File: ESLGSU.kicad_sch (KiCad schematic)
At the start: 3 parts, among them J1 Barrel_Jack_Switch, U1 TCA9544A

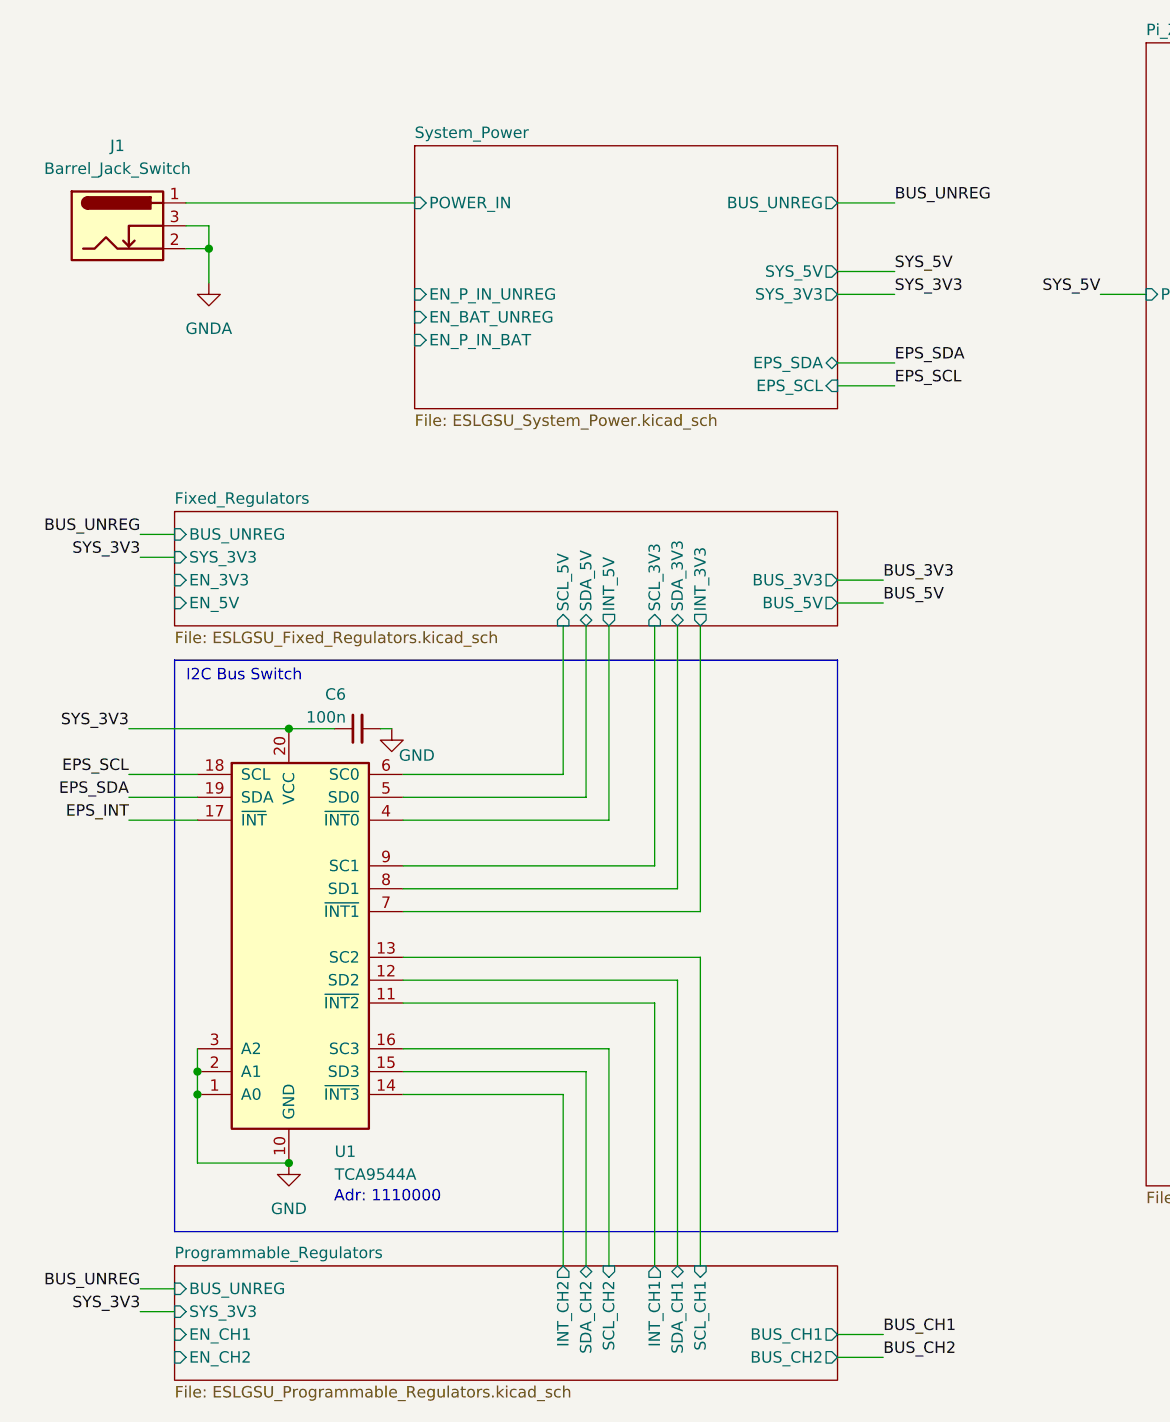
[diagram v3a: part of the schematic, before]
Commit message: Added 5v/3V3 regulators and mux
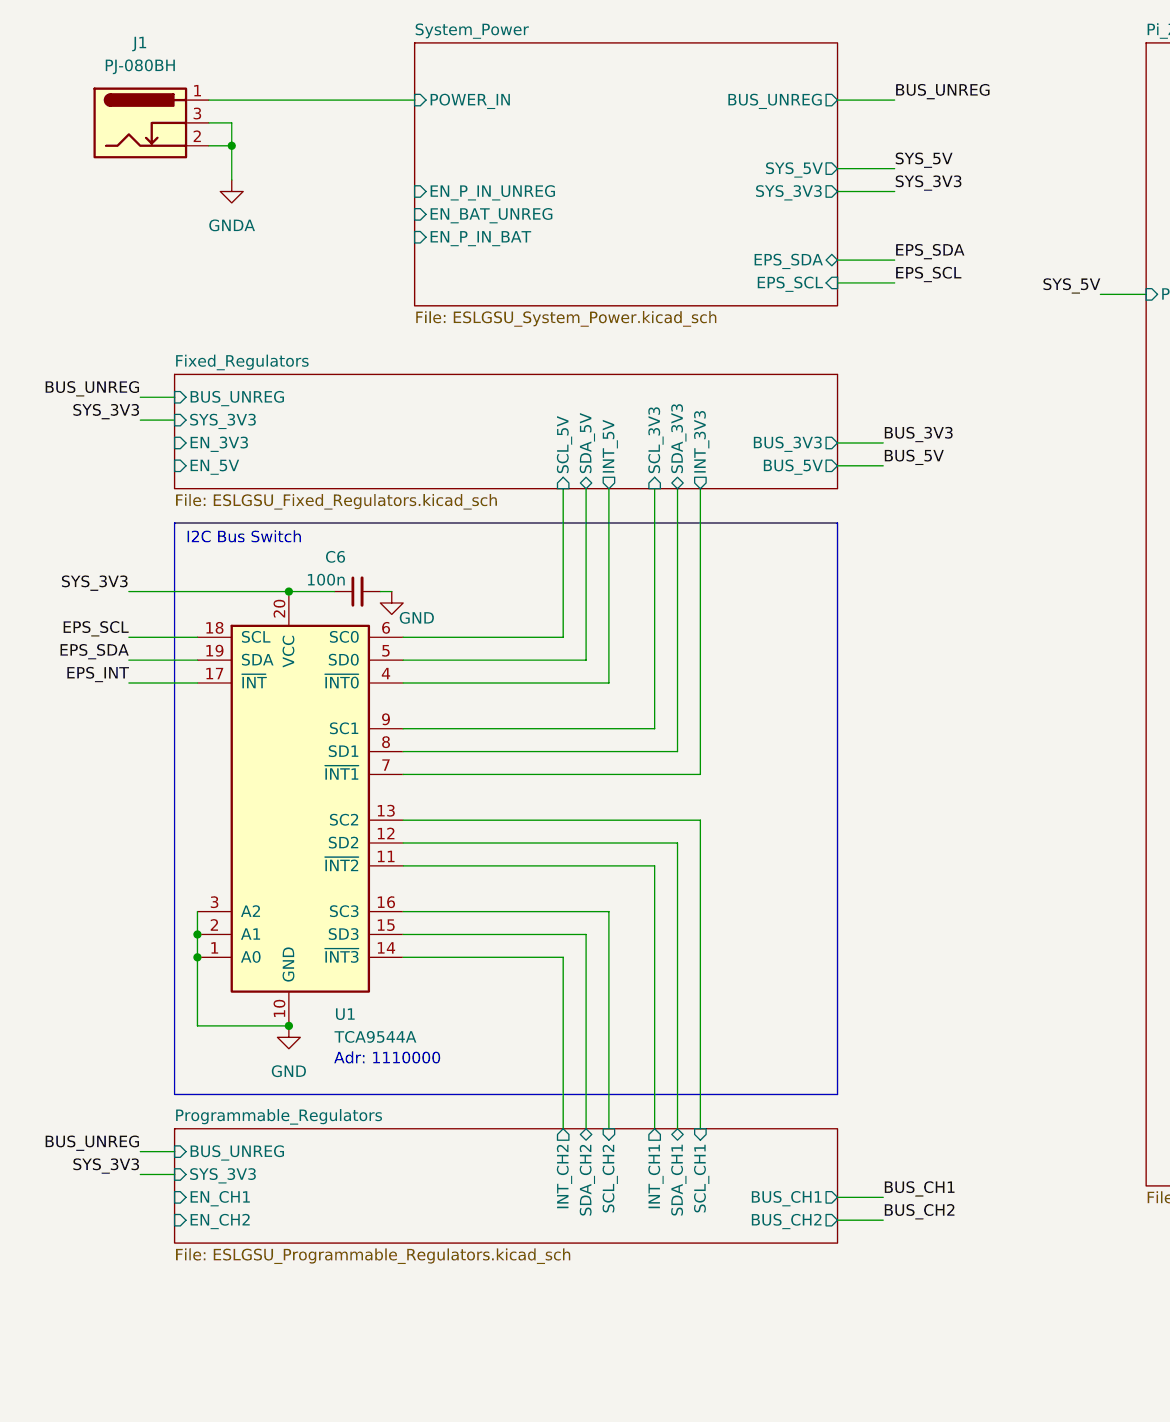
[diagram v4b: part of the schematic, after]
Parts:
- J1: value Barrel_Jack_Switch -> PJ-080BH
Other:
- moved on the sheet: C6, J1, U1

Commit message: Tried to prepare for order
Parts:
- U1: value TCA9544A -> TCA9544APWR
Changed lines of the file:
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@@
       (effects (font (size 1.27 1.27)) (justify left))
     )
-    (property "Value" "TCA9544A" (at 62.23 135.89 0)
+    (property "Value" "TCA9544APWR" (at 62.23 135.89 0)
       (effects (font (size 1.27 1.27)) (justify left))
     )

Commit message: Schematic work
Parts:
- C6: footprint Capacitor_SMD:C_0603_1608Metric -> Capacitor_SMD:C_0402_1005Metric; LCSC Part (none) -> C307331
- U1: LCSC Part (none) -> C2674619
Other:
- added sheet Misc_uCs1 (ESLGSU_Misc_uCs.kicad_sch)
- sheet Misc_uCs ports: added BOOTLDR, CAN1_H, CAN1_L, GPIO_1, GPIO_2, GPIO_3, GPIO_4, I2C1_SCL, I2C1_SDA, PISER_RX, PISER_TX, PISPI_MISO, PISPI_MOSI, PISPI_NSS, PISPI_SCK, SYS_3V3, SYS_5V, nRST; removed none

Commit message: Second last bit of schematic work
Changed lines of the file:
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@@
+    (stroke (width 0) (type default))
+  )
+  (wire (pts (xy 199.39 83.82) (xy 203.2 83.82))
+    (stroke (width 0) (type default))
+  )
+  (wire (pts (xy 223.52 171.45) (xy 227.33 171.45))
     (stroke (width 0) (type default))
   )
@@
     (stroke (width 0) (type default))
   )
+  (wire (pts (xy 223.52 189.23) (xy 227.33 189.23))
+    (stroke (width 0) (type default))
+  )
   (wire (pts (xy 50.8 40.64) (xy 50.8 36.83))
     (stroke (width 0) (type default))
@@
     (stroke (width 0) (type default))
   )
+  (wire (pts (xy 223.52 176.53) (xy 227.33 176.53))
+    (stroke (width 0) (type default))
+  )
   (wire (pts (xy 90.17 93.98) (xy 90.17 74.93))
     (stroke (width 0) (type default))
@@
     (stroke (width 0) (type default))
   )
+  (wire (pts (xy 199.39 81.28) (xy 203.2 81.28))
+    (stroke (width 0) (type default))
+  )
+  (wire (pts (xy 223.52 163.83) (xy 227.33 163.83))
+    (stroke (width 0) (type default))
+  )
   (wire (pts (xy 69.85 111.76) (xy 102.87 111.76))
     (stroke (width 0) (type default))
@@
     (stroke (width 0) (type default))
   )
+  (wire (pts (xy 223.52 181.61) (xy 227.33 181.61))
+    (stroke (width 0) (type default))
+  )
   (wire (pts (xy 223.52 144.78) (xy 227.33 144.78))
     (stroke (width 0) (type default))
   )
+  (wire (pts (xy 223.52 127) (xy 227.33 127))
+    (stroke (width 0) (type default))
+  )
   (wire (pts (xy 62.23 86.36) (xy 57.15 86.36))
     (stroke (width 0) (type default))
@@
     (stroke (width 0) (type default))
   )
+  (wire (pts (xy 223.52 173.99) (xy 227.33 173.99))
+    (stroke (width 0) (type default))
+  )
   (wire (pts (xy 118.11 31.75) (xy 124.46 31.75))
     (stroke (width 0) (type default))
@@
     (stroke (width 0) (type default))
   )
+  (wire (pts (xy 223.52 166.37) (xy 227.33 166.37))
+    (stroke (width 0) (type default))
+  )
   (wire (pts (xy 118.11 49.53) (xy 124.46 49.53))
     (stroke (width 0) (type default))
   )
+  (wire (pts (xy 223.52 124.46) (xy 227.33 124.46))
+    (stroke (width 0) (type default))
+  )
   (wire (pts (xy 69.85 124.46) (xy 90.17 124.46))
     (stroke (width 0) (type default))
@@
     (stroke (width 0) (type default))
   )
+  (wire (pts (xy 223.52 179.07) (xy 227.33 179.07))
+    (stroke (width 0) (type default))
+  )
   (wire (pts (xy 223.52 142.24) (xy 227.33 142.24))
     (stroke (width 0) (type default))
@@
     (stroke (width 0) (type default))
   )
+  (wire (pts (xy 199.39 86.36) (xy 203.2 86.36))
+    (stroke (width 0) (type default))
+  )
+  (wire (pts (xy 223.52 184.15) (xy 227.33 184.15))
+    (stroke (width 0) (type default))
+  )
   (wire (pts (xy 92.71 146.05) (xy 92.71 121.92))
     (stroke (width 0) (type default))
   )
+  (wire (pts (xy 223.52 186.69) (xy 227.33 186.69))
+    (stroke (width 0) (type default))
+  )
   (wire (pts (xy 46.99 134.62) (xy 57.15 134.62))
     (stroke (width 0) (type default))
@@
     (effects (font (size 1.27 1.27)) (justify left bottom))
   )
+  (label "SYS_5V" (at 223.52 124.46 180) (fields_autoplaced)
+    (effects (font (size 1.27 1.27)) (justify right bottom))
+  )
+  (label "PISER_RX" (at 223.52 189.23 180) (fields_autoplaced)
+    (effects (font (size 1.27 1.27)) (justify right bottom))
+  )
+  (label "PISPI_MOSI" (at 223.52 181.61 180) (fields_autoplaced)
+    (effects (font (size 1.27 1.27)) (justify right bottom))
+  )
+  (label "SYS_3V3" (at 223.52 127 180) (fields_autoplaced)
+    (effects (font (size 1.27 1.27)) (justify right bottom))
+  )
+  (label "PI_nRST_MISC2" (at 223.52 173.99 180) (fields_autoplaced)
+    (effects (font (size 1.27 1.27)) (justify right bottom))
+  )
   (label "BUS_UNREG" (at 40.64 148.59 180) (fields_autoplaced)
     (effects (font (size 1.27 1.27)) (justify right bottom))
@@
     (effects (font (size 1.27 1.27)) (justify left bottom))
   )
+  (label "PI_nRST_MISC2" (at 203.2 83.82 0) (fields_autoplaced)
+    (effects (font (size 1.27 1.27)) (justify left bottom))
+  )
   (label "PISER_RX" (at 203.2 127 0) (fields_autoplaced)
     (effects (font (size 1.27 1.27)) (justify left bottom))
   )
+  (label "PI_SS_MISC2" (at 203.2 81.28 0) (fields_autoplaced)
+    (effects (font (size 1.27 1.27)) (justify left bottom))
+  )
   (label "PI_SS_MISC1" (at 203.2 67.31 0) (fields_autoplaced)
     (effects (font (size 1.27 1.27)) (justify left bottom))
@@
     (effects (font (size 1.27 1.27)) (justify left bottom))
   )
+  (label "PISPI_SCK" (at 223.52 179.07 180) (fields_autoplaced)
+    (effects (font (size 1.27 1.27)) (justify right bottom))
+  )
   (label "PI_nRST_MISC1" (at 223.52 134.62 180) (fields_autoplaced)
     (effects (font (size 1.27 1.27)) (justify right bottom))
@@
     (effects (font (size 1.27 1.27)) (justify left bottom))
   )
+  (label "PISPI_MISO" (at 223.52 184.15 180) (fields_autoplaced)
+    (effects (font (size 1.27 1.27)) (justify right bottom))
+  )
   (label "PI_SS_MISC1" (at 223.52 137.16 180) (fields_autoplaced)
     (effects (font (size 1.27 1.27)) (justify right bottom))
@@
     (effects (font (size 1.27 1.27)) (justify right bottom))
   )
+  (label "SYS_3V3" (at 223.52 166.37 180) (fields_autoplaced)
+    (effects (font (size 1.27 1.27)) (justify right bottom))
+  )
+  (label "PI_BOOTLDR_MISC2" (at 223.52 171.45 180) (fields_autoplaced)
+    (effects (font (size 1.27 1.27)) (justify right bottom))
+  )
   (label "SYS_5V" (at 124.46 39.37 0) (fields_autoplaced)
     (effects (font (size 1.27 1.27)) (justify left bottom))
   )
+  (label "PI_BOOTLDR_MISC2" (at 203.2 86.36 0) (fields_autoplaced)
+    (effects (font (size 1.27 1.27)) (justify left bottom))
+  )
+  (label "PI_SS_MISC2" (at 223.52 176.53 180) (fields_autoplaced)
+    (effects (font (size 1.27 1.27)) (justify right bottom))
+  )
   (label "BUS_3V3" (at 123.19 69.85 0) (fields_autoplaced)
     (effects (font (size 1.27 1.27)) (justify left bottom))
@@
     (effects (font (size 1.27 1.27)) (justify right bottom))
   )
+  (label "PISER_TX" (at 223.52 186.69 180) (fields_autoplaced)
+    (effects (font (size 1.27 1.27)) (justify right bottom))
+  )
   (label "EPS_SCL" (at 39.37 91.44 180) (fields_autoplaced)
     (effects (font (size 1.27 1.27)) (justify right bottom))
   )
+  (label "SYS_5V" (at 223.52 163.83 180) (fields_autoplaced)
+    (effects (font (size 1.27 1.27)) (justify right bottom))
+  )

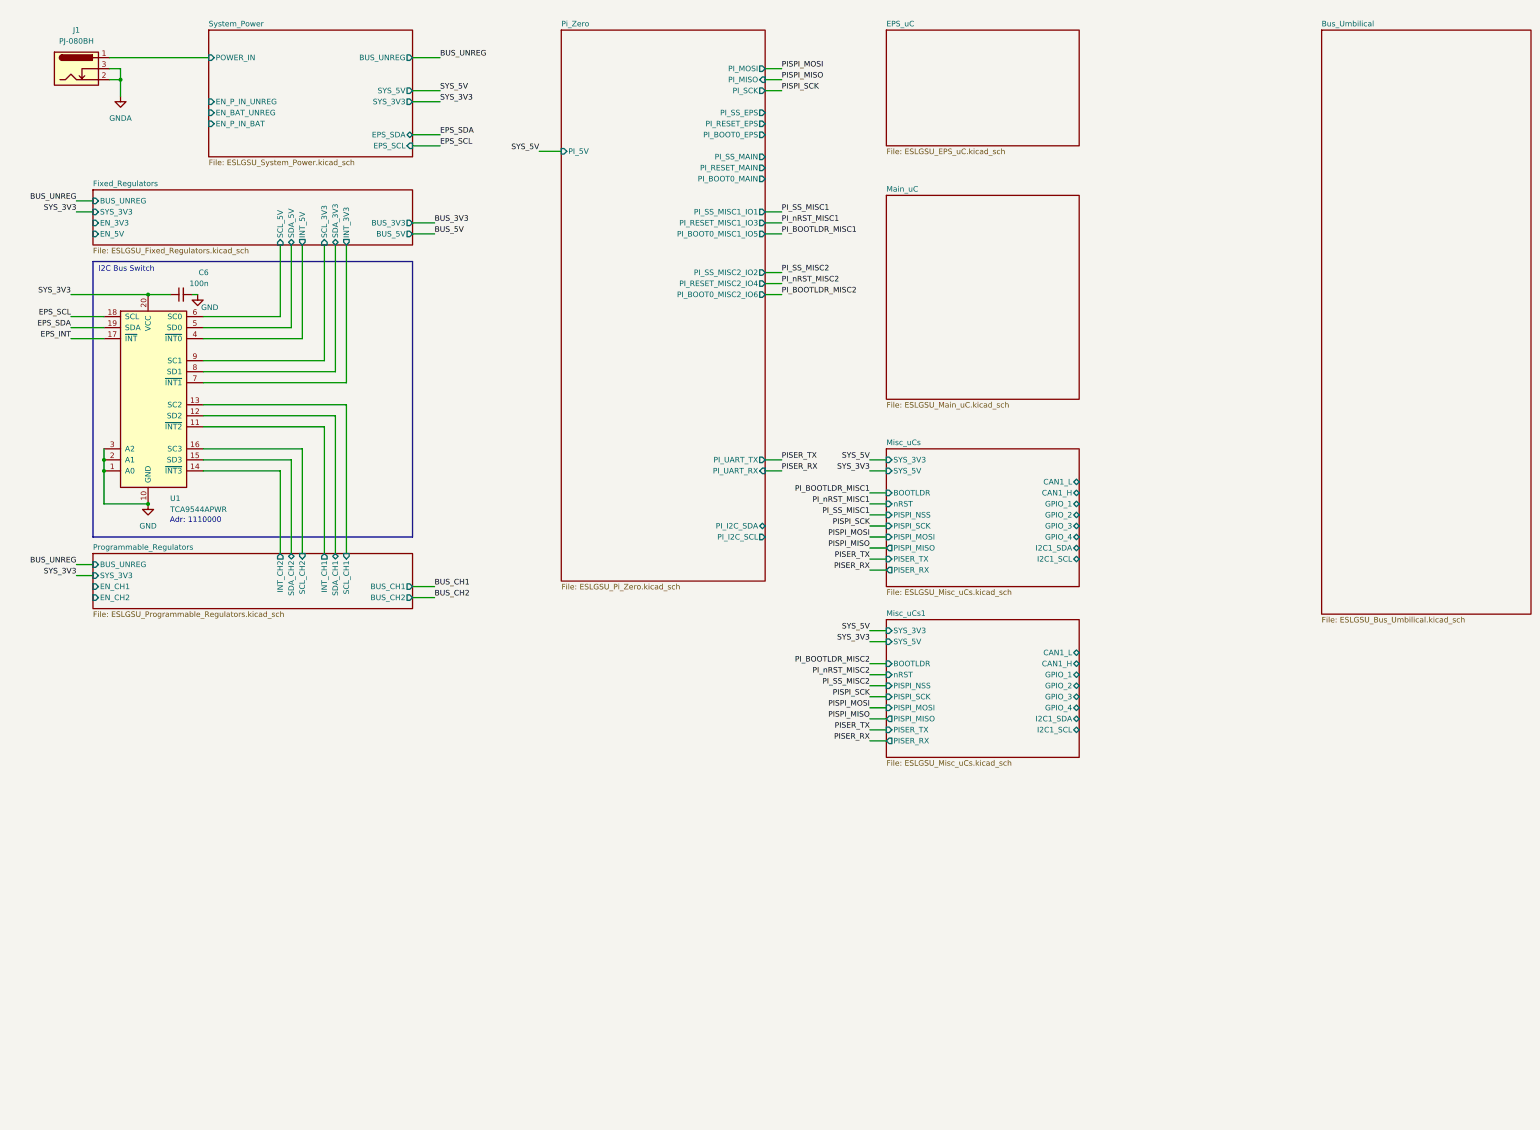
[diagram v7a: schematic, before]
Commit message: Final schematic work, added battery charger, linked everything up
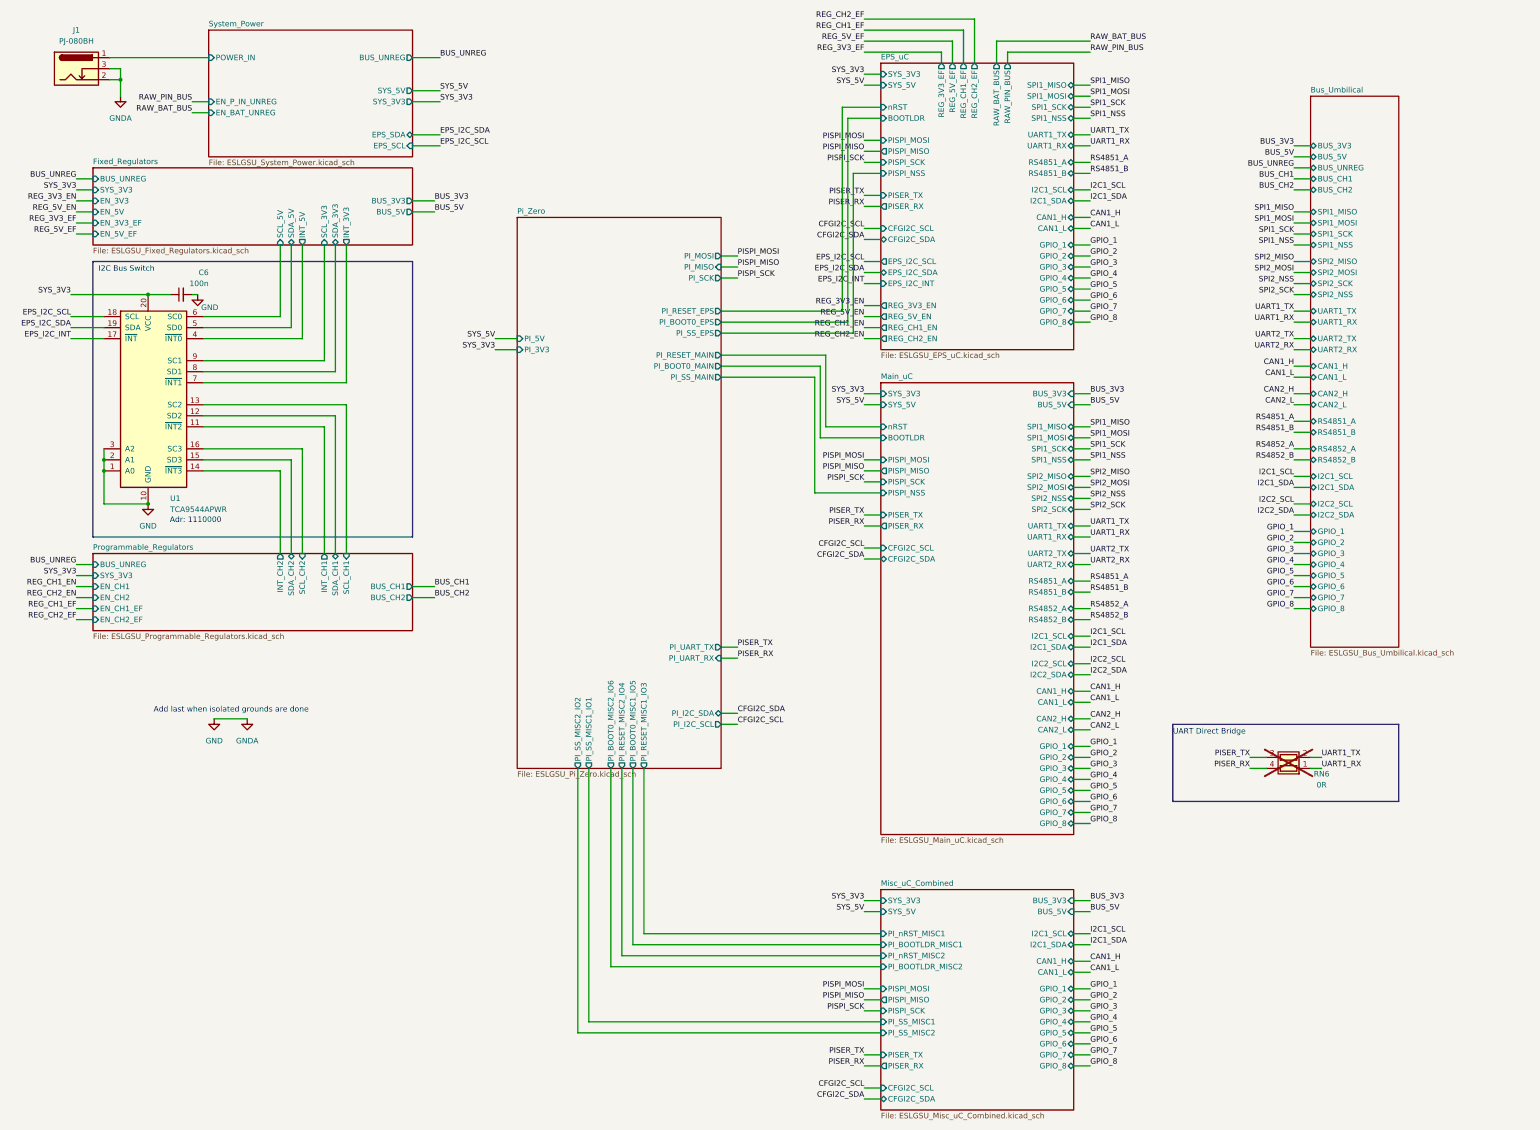
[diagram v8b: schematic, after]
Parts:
- added RN6: 0R, Resistor_SMD:R_Array_Convex_2x0402, symbol Device:R_Pack02
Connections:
- net GNDA is gone; now on net GND: J1.2, J1.3
- net PISER_RX: now also RN6.4 (R1.2)
- net PISER_TX: now also RN6.3 (R2.2)
- net EPS_INT renamed EPS_I2C_INT
- net EPS_SCL renamed EPS_I2C_SCL
- net EPS_SDA renamed EPS_I2C_SDA
- new net UART1_RX: RN6.1 (R1.1)
- new net UART1_TX: RN6.2 (R2.1)
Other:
- removed sheet Misc_uCs
- removed sheet Misc_uCs1
- added sheet Misc_uC_Combined (ESLGSU_Misc_uC_Combined.kicad_sch)
- sheet Bus_Umbilical ports: added BUS_3V3, BUS_5V, BUS_CH1, BUS_CH2, BUS_UNREG, CAN1_H, CAN1_L, CAN2_H, CAN2_L, GPIO_1, GPIO_2, GPIO_3, GPIO_4, GPIO_5, GPIO_6, GPIO_7, GPIO_8, I2C1_SCL, I2C1_SDA, I2C2_SCL, I2C2_SDA, RS4851_A, RS4851_B, RS4852_A, RS4852_B, SPI1_MISO, SPI1_MOSI, SPI1_NSS, SPI1_SCK, SPI2_MISO, SPI2_MOSI, SPI2_NSS, SPI2_SCK, UART1_RX, UART1_TX, UART2_RX, UART2_TX; removed none
- sheet EPS_uC ports: added BOOTLDR, CAN1_H, CAN1_L, CFGI2C_SCL, CFGI2C_SDA, EPS_I2C_INT, EPS_I2C_SCL, EPS_I2C_SDA, GPIO_1, GPIO_2, GPIO_3, GPIO_4, GPIO_5, GPIO_6, GPIO_7, GPIO_8, I2C1_SCL, I2C1_SDA, PISER_RX, PISER_TX, PISPI_MISO, PISPI_MOSI, PISPI_NSS, PISPI_SCK, RAW_BAT_BUS, RAW_PIN_BUS, REG_3V3_EF, REG_3V3_EN, REG_5V_EF, REG_5V_EN, REG_CH1_EF, REG_CH1_EN, REG_CH2_EF, REG_CH2_EN, RS4851_A, RS4851_B, SPI1_MISO, SPI1_MOSI, SPI1_NSS, SPI1_SCK, SYS_3V3, SYS_5V, UART1_RX, UART1_TX, nRST; removed none
- sheet Fixed_Regulators ports: added EN_3V3_EF, EN_5V_EF; removed none
- sheet Main_uC ports: added BOOTLDR, BUS_3V3, BUS_5V, CAN1_H, CAN1_L, CAN2_H, CAN2_L, CFGI2C_SCL, CFGI2C_SDA, GPIO_1, GPIO_2, GPIO_3, GPIO_4, GPIO_5, GPIO_6, GPIO_7, GPIO_8, I2C1_SCL, I2C1_SDA, I2C2_SCL, I2C2_SDA, PISER_RX, PISER_TX, PISPI_MISO, PISPI_MOSI, PISPI_NSS, PISPI_SCK, RS4851_A, RS4851_B, RS4852_A, RS4852_B, SPI1_MISO, SPI1_MOSI, SPI1_NSS, SPI1_SCK, SPI2_MISO, SPI2_MOSI, SPI2_NSS, SPI2_SCK, SYS_3V3, SYS_5V, UART1_RX, UART1_TX, UART2_RX, UART2_TX, nRST; removed none
- sheet Pi_Zero ports: added PI_3V3; removed none
- sheet Programmable_Regulators ports: added EN_CH1_EF, EN_CH2_EF; removed none
- sheet System_Power ports: added none; removed EN_P_IN_BAT
- note added: "Add last when isolated grounds are done"
- note added: "UART Direct Bridge"
